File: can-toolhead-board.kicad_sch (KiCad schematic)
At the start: 40 parts, among them J1 MF3-2x2P, J2 USB_C_Receptacle_USB2.0, J3 SH-6P, SW1 SW_Push, SW2 SW_Push, U1 TPS62933, U2 MIC5365-3.3YC5, U3 TJA1051TK-3, U4 STM32G0B1KBU6, U7 USBLC6-2P6

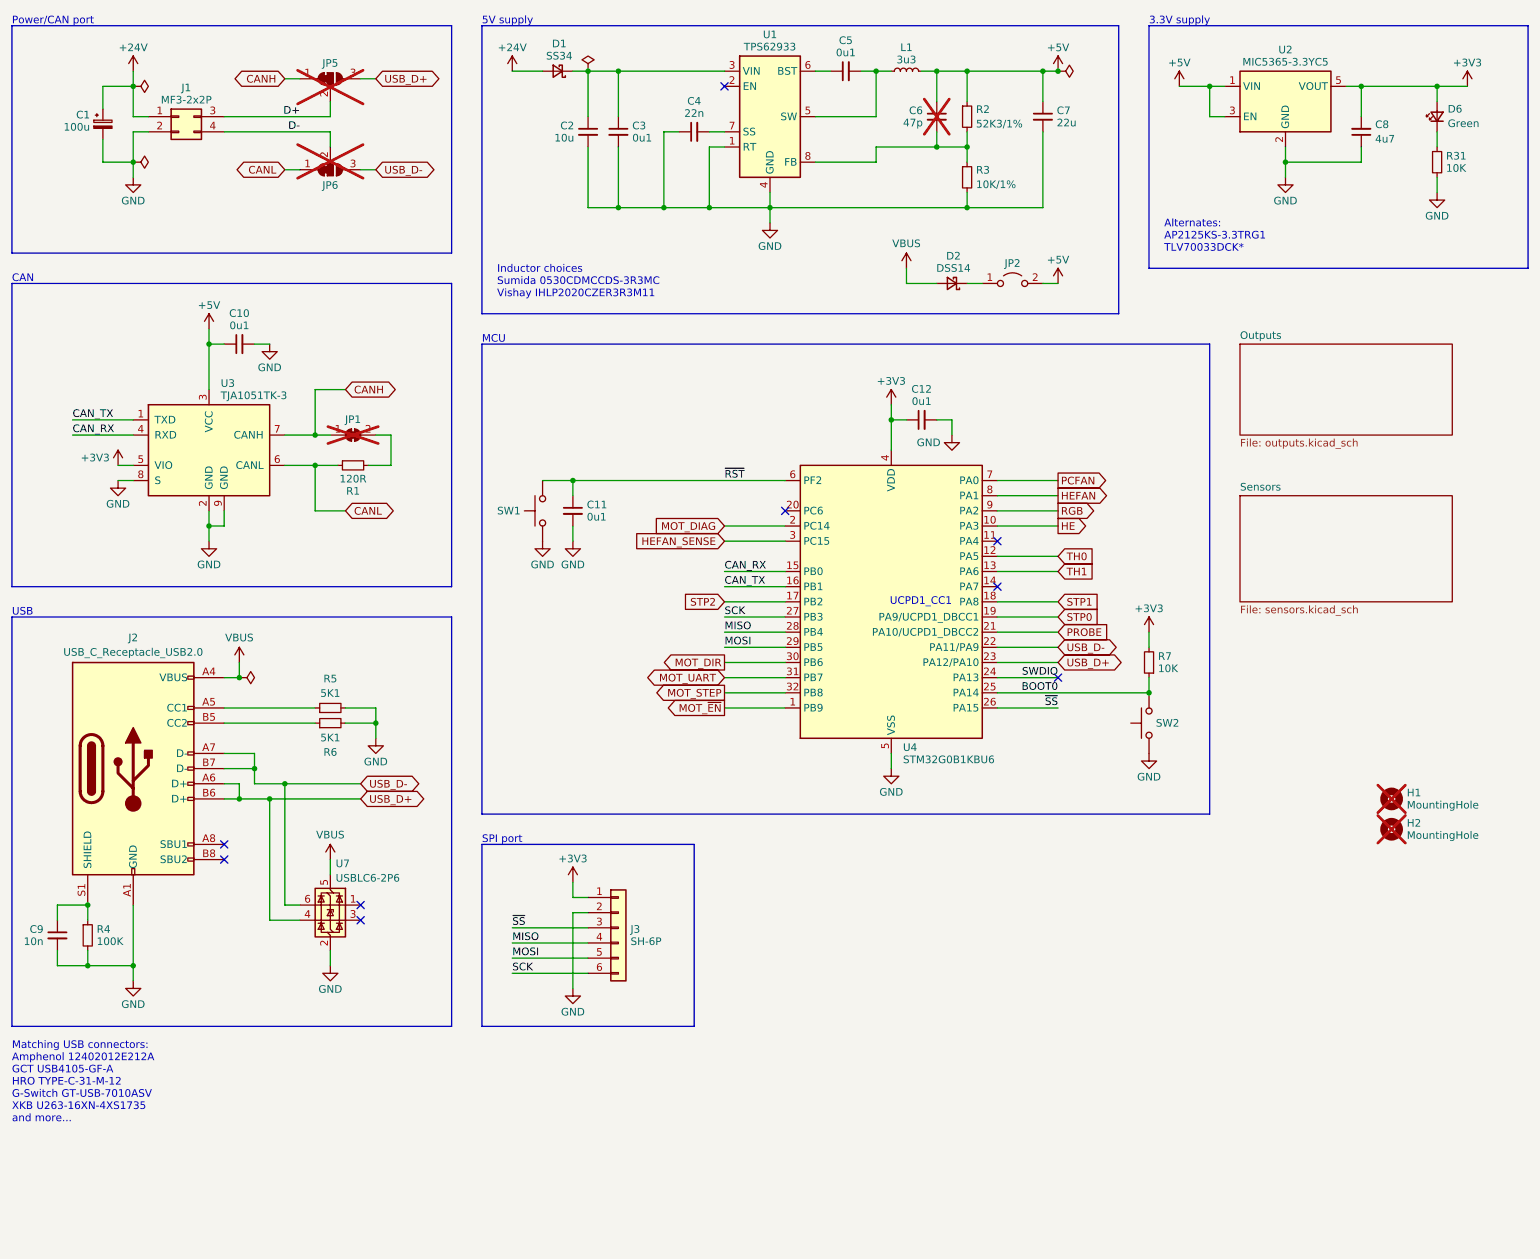
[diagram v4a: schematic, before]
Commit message: Remove DNP from stuff where it doesn't belong in the schematic. Also DNP the fan port caps (the BOM ones weren't rated good for 24V anyway), but in any case since I couldn't find 4.7uF/35V/0603 good for 105C, reduce them to 2.2uF. Too bad I didn't make them 0805
Also added note for higher temp STM32, so I think all the components
should be good to 105C, except for the JST connectors...
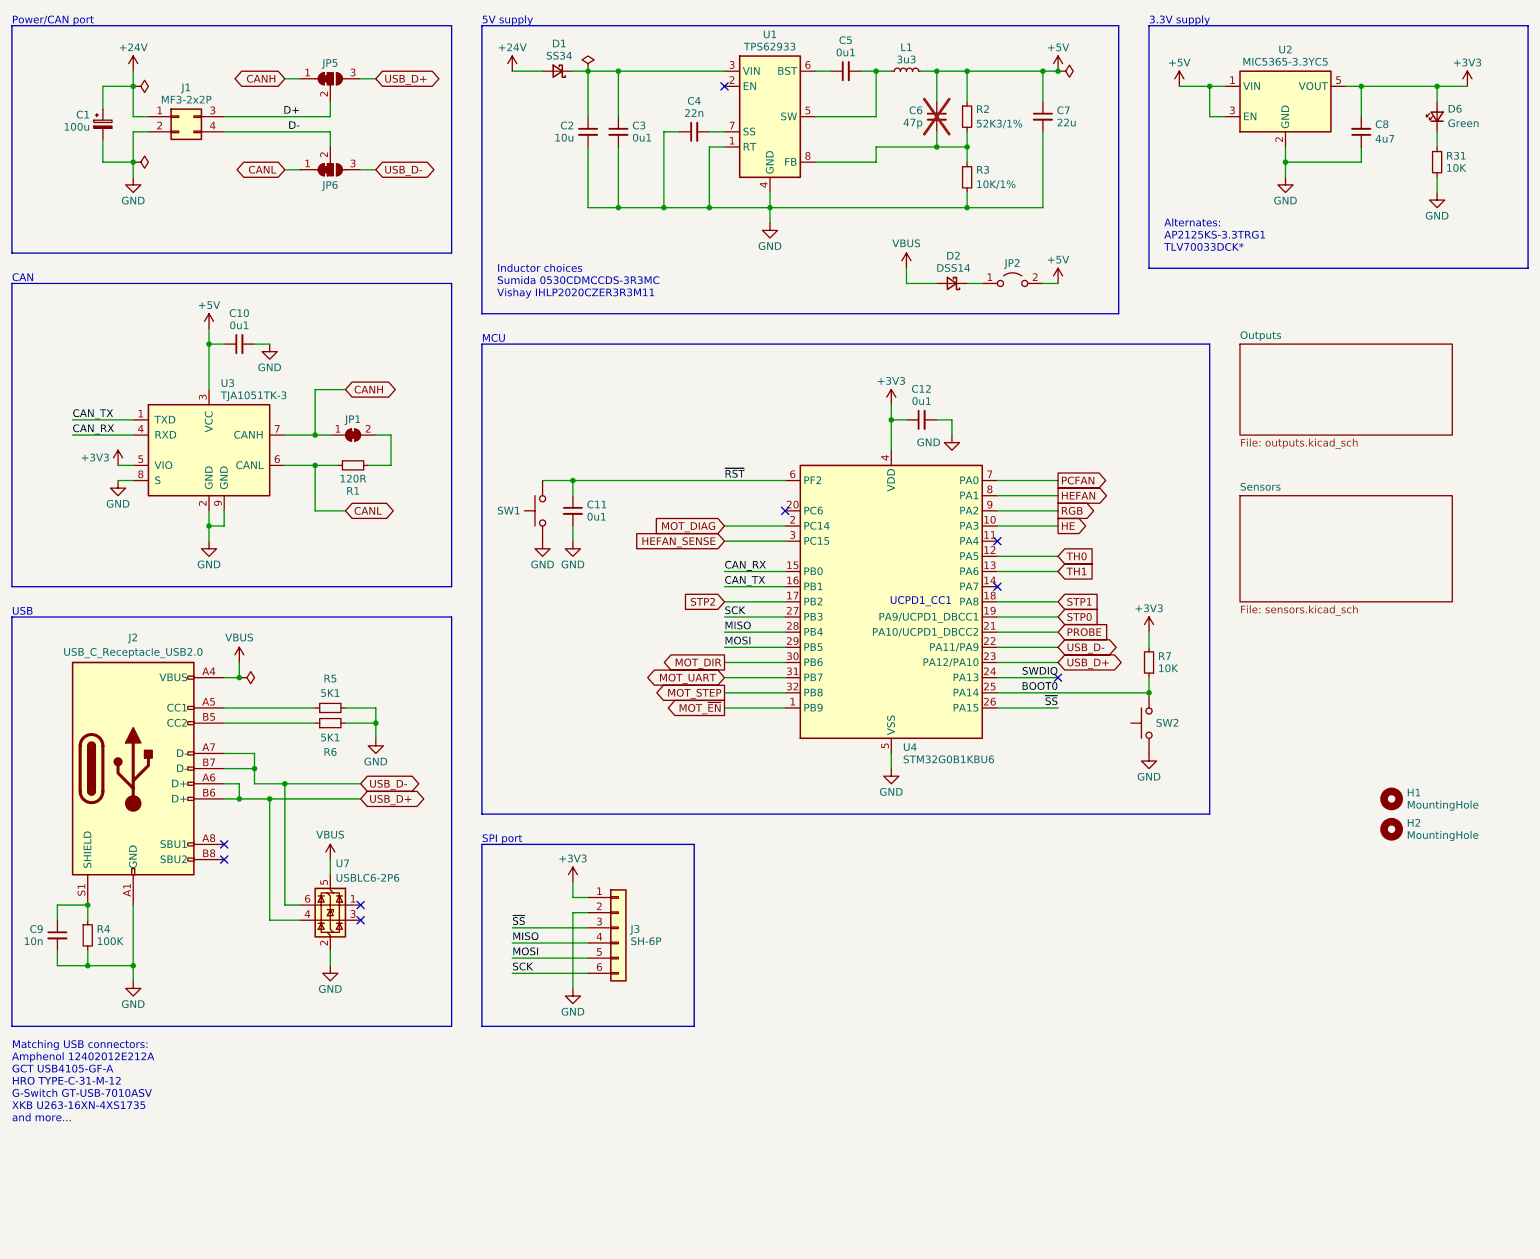
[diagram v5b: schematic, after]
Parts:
- C1: Notes (none) -> 35V electrolytic
- C10, C11, C12, C3, C5: Notes (none) -> 50V
- C2: Notes (none) -> 35V X7T
- C7: Notes (none) -> 10V X6S
- H1, H2, JP1, JP5, JP6: now fitted
- U4: Notes (none) -> Use STM32G0B1KxU7 for 105C temperature rating

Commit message: Fix LCSC part for 74LVC2G17 (wrong package). List alternate parts in notes fields.
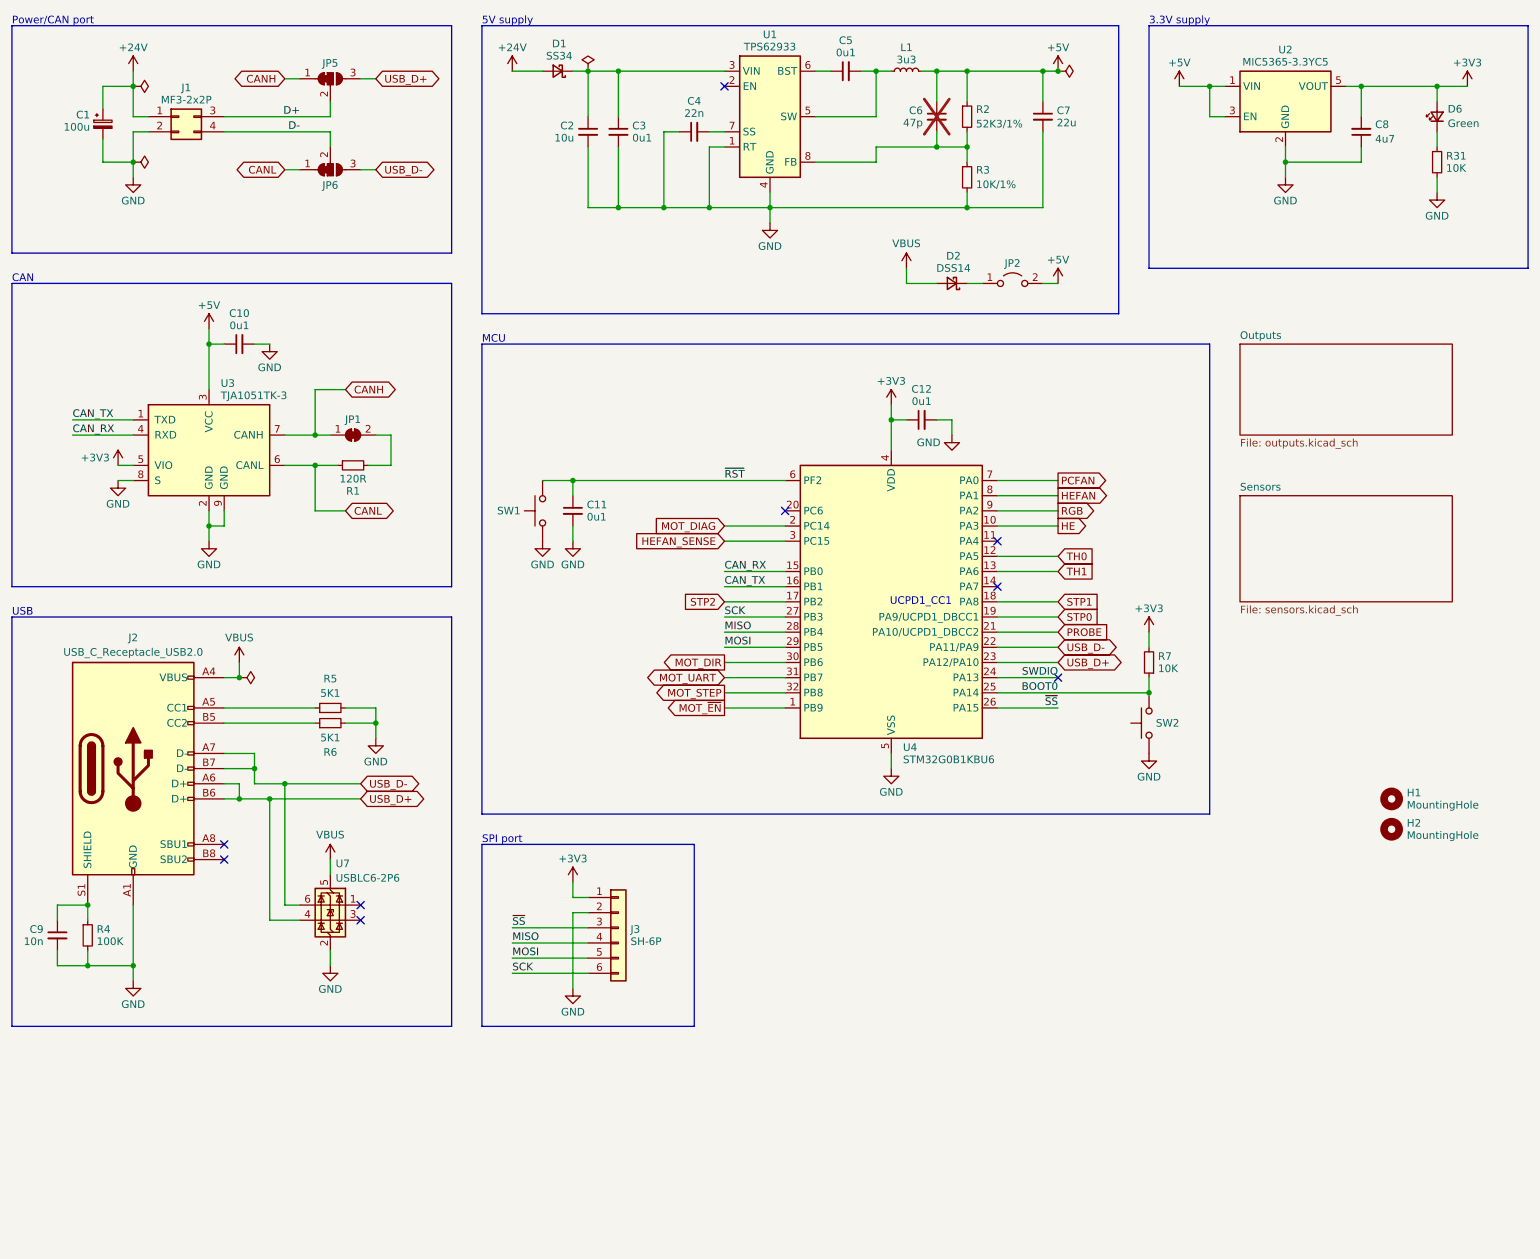
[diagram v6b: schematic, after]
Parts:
- J2: Notes (none) -> Alternates: Amphenol 12402012E212A, GCT USB4105-GF-A, HRO T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
- JP2: LCSC C6837593;C5274553 -> C706997;C5274553
- L1: Notes (none) -> Alternates: Sumida 0530CDMCCDS-3R3MC
- U2: Notes (none) -> Alternates: TLV70033DCKx, AP2125KS-3.3TRG1; manf# TLV70033DCKR -> MIC5365-3.3YC5-TR
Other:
- note removed: "Alternates: AP2125KS-3.3TRG1 TLV70033DCK*"
- note removed: "Inductor choices Sumida 0530CDMCCDS-3R3MC Vishay IHLP2020CZER3R3M11"
- note removed: "Matching USB connectors: Amphenol 12402012E212A GCT USB4105-GF-A HRO TYPE-C-31-M-12 G-Switch GT-USB-7010ASV XKB U263-16XN-4XS1735 and more..."
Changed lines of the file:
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@@
 		)
 	)
-	(text "Matching USB connectors:\nAmphenol 12402012E212A\nGCT USB4105-GF-A\nHRO TYPE-C-31-M-12\nG-Switch GT-USB-7010ASV\nXKB U263-16XN-4XS1735\nand more..."
-		(exclude_from_sim no)
-		(at 22.86 193.04 0)
-		(effects
-			(font
-				(size 1.27 1.27)
-			)
-			(justify left top)
-		)
-	)
-	(text "Alternates:\nAP2125KS-3.3TRG1\nTLV70033DCK*"
-		(exclude_from_sim no)
-		(at 215.9 60.96 0)
-		(effects
-			(font
-				(size 1.27 1.27)
-			)
-			(justify left bottom)
-		)
-	)
 	(text "SPI port"
 		(exclude_from_sim no)
@@
 		)
 	)
-	(text "Inductor choices\nSumida 0530CDMCCDS-3R3MC\nVishay IHLP2020CZER3R3M11"
-		(exclude_from_sim no)
-		(at 104.14 68.58 0)
-		(effects
-			(font
-				(size 1.27 1.27)
-			)
-			(justify left bottom)
-		)
-	)
 	(label "MISO"
 		(at 106.68 176.53 0)
@@
 			)
 		)
-		(property "Datasheet" "~"
+		(property "Datasheet" "https://www.smc-diodes.com/propdf/DSS12U%20THRU%20DSS125U%20N1873%20REV.A.pdf"
 			(at 180.34 66.04 90)
 			(effects
@@
 			)
 		)
-		(property "Datasheet" "~"
+		(property "Datasheet" "https://diotec.com/request/datasheet/sk34sma-3g.pdf"
 			(at 114.3 30.48 90)
 			(effects
@@
 			)
 		)
-		(property "Notes" ""
+		(property "Notes" "Alternates: Amphenol 12402012E212A, GCT USB4105-GF-A, HRO TYPE-C-31-M-12, G-Switch GT-USB-7010ASV, XKB U263-16XN-4XS1735"
 			(at 43.18 147.32 0)
 			(effects
@@
 			)
 		)
-		(property "LCSC" "C6837593;C5274553"
+		(property "LCSC" "C706997;C5274553"
 			(at 190.5 66.04 0)
 			(effects
@@
 			)
 		)
-		(property "Notes" ""
+		(property "Notes" "Alternates: Sumida 0530CDMCCDS-3R3MC"
 			(at 172.72 30.48 0)
 			(effects
@@
 			)
 		)
-		(property "manf#" "TLV70033DCKR"
+		(property "manf#" "MIC5365-3.3YC5-TR"
 			(at 236.22 35.56 0)
 			(effects
@@
 			)
 		)
-		(property "Notes" ""
+		(property "Notes" "Alternates: TLV70033DCKx, AP2125KS-3.3TRG1"
 			(at 236.22 35.56 0)
 			(effects
